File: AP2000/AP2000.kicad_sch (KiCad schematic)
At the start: 6 parts

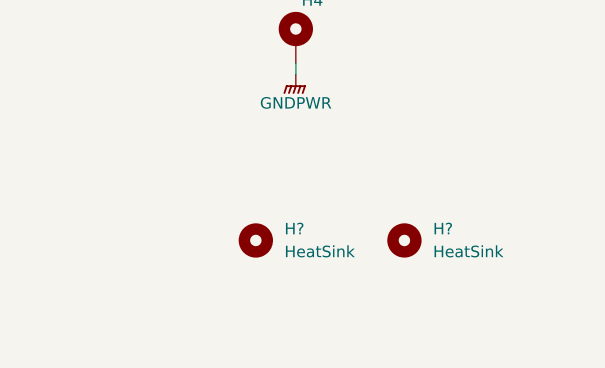
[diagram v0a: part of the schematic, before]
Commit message: Mods to AP2000 for manufacturing. 50 PCBs ordered from JLCPCB with SMd assembly.
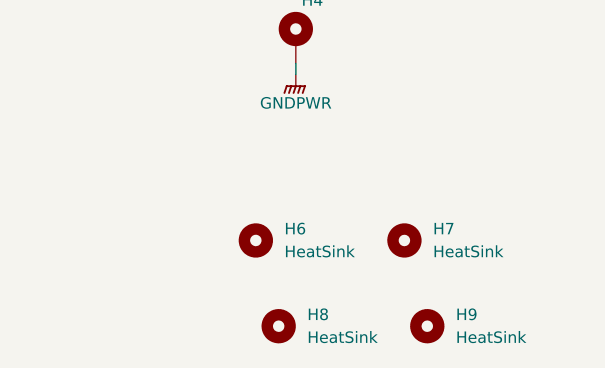
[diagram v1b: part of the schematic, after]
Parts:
- added H8, H9: HeatSink, Scott:CM4_Mounting_Hole, symbol Mechanical:MountingHole
- H1: value Mounting Hole -> HeatSink
- gave numbers to parts that had none: 2
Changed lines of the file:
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@@
   (symbol (lib_id "Mechanical:MountingHole") (at 213.995 141.605 0) (unit 1)
     (in_bom yes) (on_board yes) (fields_autoplaced)
-    (property "Reference" "H?" (id 0) (at 217.17 140.3349 0)
+    (property "Reference" "H6" (id 0) (at 217.17 140.3349 0)
       (effects (font (size 1.27 1.27)) (justify left))
     )
@@
     )
     (property "Datasheet" "https://www.amazon.com/MroMax-Machine-Phillips-Stainless-Cabinet/dp/B07YS6D2GT/ref=sr_1_10?dchild=1&gclid=Cj0KCQjwqKuKBhCxARIsACf4XuF4Q-bwWlCSQ9m9de-DMcRwzY4OKs2FQ95kiMNENXwpyLO88pn_MmwaAvo_EALw_wcB&hvadid=503610561779&hvdev=c&hvlocphy=9028269&hvnetw=g&hvqmt=e&hvrand=9499715407067735490&hvtargid=kwd-296946281905&hydadcr=6199_9464726&keywords=m2.5+x+8mm+screws&qid=1632341243&sr=8-10" (id 3) (at 213.995 141.605 0)
+      (effects (font (size 1.27 1.27)) hide)
+    )
+  )
+  (symbol (lib_id "Mechanical:MountingHole") (at 216.535 151.13 0) (unit 1)
+    (in_bom yes) (on_board yes) (fields_autoplaced)
+    (property "Reference" "H8" (id 0) (at 219.71 149.8599 0)
+      (effects (font (size 1.27 1.27)) (justify left))
+    )
+    (property "Value" "HeatSink" (id 1) (at 219.71 152.3999 0)
+      (effects (font (size 1.27 1.27)) (justify left))
+    )
+    (property "Footprint" "Scott:CM4_Mounting_Hole" (id 2) (at 216.535 151.13 0)
+      (effects (font (size 1.27 1.27)) hide)
+    )
+    (property "Datasheet" "https://www.amazon.com/MroMax-Machine-Phillips-Stainless-Cabinet/dp/B07YS6D2GT/ref=sr_1_10?dchild=1&gclid=Cj0KCQjwqKuKBhCxARIsACf4XuF4Q-bwWlCSQ9m9de-DMcRwzY4OKs2FQ95kiMNENXwpyLO88pn_MmwaAvo_EALw_wcB&hvadid=503610561779&hvdev=c&hvlocphy=9028269&hvnetw=g&hvqmt=e&hvrand=9499715407067735490&hvtargid=kwd-296946281905&hydadcr=6199_9464726&keywords=m2.5+x+8mm+screws&qid=1632341243&sr=8-10" (id 3) (at 216.535 151.13 0)
       (effects (font (size 1.27 1.27)) hide)
     )
@@
   (symbol (lib_id "Mechanical:MountingHole") (at 230.505 141.605 0) (unit 1)
     (in_bom yes) (on_board yes) (fields_autoplaced)
-    (property "Reference" "H?" (id 0) (at 233.68 140.3349 0)
+    (property "Reference" "H7" (id 0) (at 233.68 140.3349 0)
       (effects (font (size 1.27 1.27)) (justify left))
     )
@@
     )
     (property "Datasheet" "https://www.amazon.com/MroMax-Machine-Phillips-Stainless-Cabinet/dp/B07YS6D2GT/ref=sr_1_10?dchild=1&gclid=Cj0KCQjwqKuKBhCxARIsACf4XuF4Q-bwWlCSQ9m9de-DMcRwzY4OKs2FQ95kiMNENXwpyLO88pn_MmwaAvo_EALw_wcB&hvadid=503610561779&hvdev=c&hvlocphy=9028269&hvnetw=g&hvqmt=e&hvrand=9499715407067735490&hvtargid=kwd-296946281905&hydadcr=6199_9464726&keywords=m2.5+x+8mm+screws&qid=1632341243&sr=8-10" (id 3) (at 230.505 141.605 0)
+      (effects (font (size 1.27 1.27)) hide)
+    )
+  )
+  (symbol (lib_id "Mechanical:MountingHole") (at 233.045 151.13 0) (unit 1)
+    (in_bom yes) (on_board yes) (fields_autoplaced)
+    (property "Reference" "H9" (id 0) (at 236.22 149.8599 0)
+      (effects (font (size 1.27 1.27)) (justify left))
+    )
+    (property "Value" "HeatSink" (id 1) (at 236.22 152.3999 0)
+      (effects (font (size 1.27 1.27)) (justify left))
+    )
+    (property "Footprint" "Scott:CM4_Mounting_Hole" (id 2) (at 233.045 151.13 0)
+      (effects (font (size 1.27 1.27)) hide)
+    )
+    (property "Datasheet" "https://www.amazon.com/MroMax-Machine-Phillips-Stainless-Cabinet/dp/B07YS6D2GT/ref=sr_1_10?dchild=1&gclid=Cj0KCQjwqKuKBhCxARIsACf4XuF4Q-bwWlCSQ9m9de-DMcRwzY4OKs2FQ95kiMNENXwpyLO88pn_MmwaAvo_EALw_wcB&hvadid=503610561779&hvdev=c&hvlocphy=9028269&hvnetw=g&hvqmt=e&hvrand=9499715407067735490&hvtargid=kwd-296946281905&hydadcr=6199_9464726&keywords=m2.5+x+8mm+screws&qid=1632341243&sr=8-10" (id 3) (at 233.045 151.13 0)
       (effects (font (size 1.27 1.27)) hide)
     )
@@
       (effects (font (size 1.27 1.27)) (justify left))
     )
-    (property "Value" "Mounting Hole" (id 1) (at 230.505 107.315 0)
+    (property "Value" "HeatSink" (id 1) (at 230.505 107.315 0)
       (effects (font (size 1.27 1.27)) (justify left) hide)
     )
@@
     )
     (path "/f3f54185-8fb0-47c3-aa5f-a619617d0618"
-      (reference "H1") (unit 1) (value "Mounting Hole") (footprint "MountingHole:MountingHole_3.7mm_Pad_TopBottom")
+      (reference "H1") (unit 1) (value "HeatSink") (footprint "MountingHole:MountingHole_3.7mm_Pad_TopBottom")
     )
     (path "/3736e4c9-a485-4284-a109-7ca11a0a21cd"
@@
       (reference "H5") (unit 1) (value "LightPipe") (footprint "Scott:VCC_LightPipe_7511A62")
     )
+    (path "/84f307bc-ff55-4060-afb7-c28adde0e26e"
+      (reference "H6") (unit 1) (value "HeatSink") (footprint "Scott:CM4_Mounting_Hole")
+    )
     (path "/5cda5b42-76c2-4977-9701-2aae3cb66034"
-      (reference "H?") (unit 1) (value "HeatSink") (footprint "Scott:CM4_Mounting_Hole")
-    )
-    (path "/84f307bc-ff55-4060-afb7-c28adde0e26e"
-      (reference "H?") (unit 1) (value "HeatSink") (footprint "Scott:CM4_Mounting_Hole")
+      (reference "H7") (unit 1) (value "HeatSink") (footprint "Scott:CM4_Mounting_Hole")
+    )
+    (path "/225b2bcc-0a8c-4181-8d76-869ceede9bf4"
+      (reference "H8") (unit 1) (value "HeatSink") (footprint "Scott:CM4_Mounting_Hole")
+    )
+    (path "/5bd193c6-8331-41c9-8310-7789aee9f513"
+      (reference "H9") (unit 1) (value "HeatSink") (footprint "Scott:CM4_Mounting_Hole")
     )
     (path "/4e123158-2d06-47e2-89a0-87bf08de438a/9ba1b965-ee46-4012-bcf5-d34cd55ad7ed"
@@
     )
     (path "/00000000-0000-0000-0000-00005cff706a/01ee700d-28fb-4df9-bfa5-8e3cd9363c82"
-      (reference "U3") (unit 1) (value "SN74LVC07AD") (footprint "Package_SO:SOIC-14_3.9x8.7mm_P1.27mm")
+      (reference "U3") (unit 1) (value "SN74LVC07AD") (footprint "Package_SO:TSSOP-14_4.4x5mm_P0.65mm")
     )
     (path "/00000000-0000-0000-0000-00005cff706a/00000000-0000-0000-0000-00005d4045a5"
@@
     )
     (path "/4e123158-2d06-47e2-89a0-87bf08de438a/3ab6118d-fc25-4dbc-a28d-ac714af62840"
-      (reference "U6") (unit 1) (value "TL431AIDBVR") (footprint "Package_TO_SOT_SMD:SOT-23-5")
+      (reference "U6") (unit 1) (value "TL431AIDBVR") (footprint "Package_TO_SOT_SMD:SOT-23")
     )
     (path "/00000000-0000-0000-0000-00005d31f999/6647051f-741c-4649-aaab-8412fec1e8f8"
